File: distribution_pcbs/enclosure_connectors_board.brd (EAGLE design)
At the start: 70 x 40 mm, 15 parts

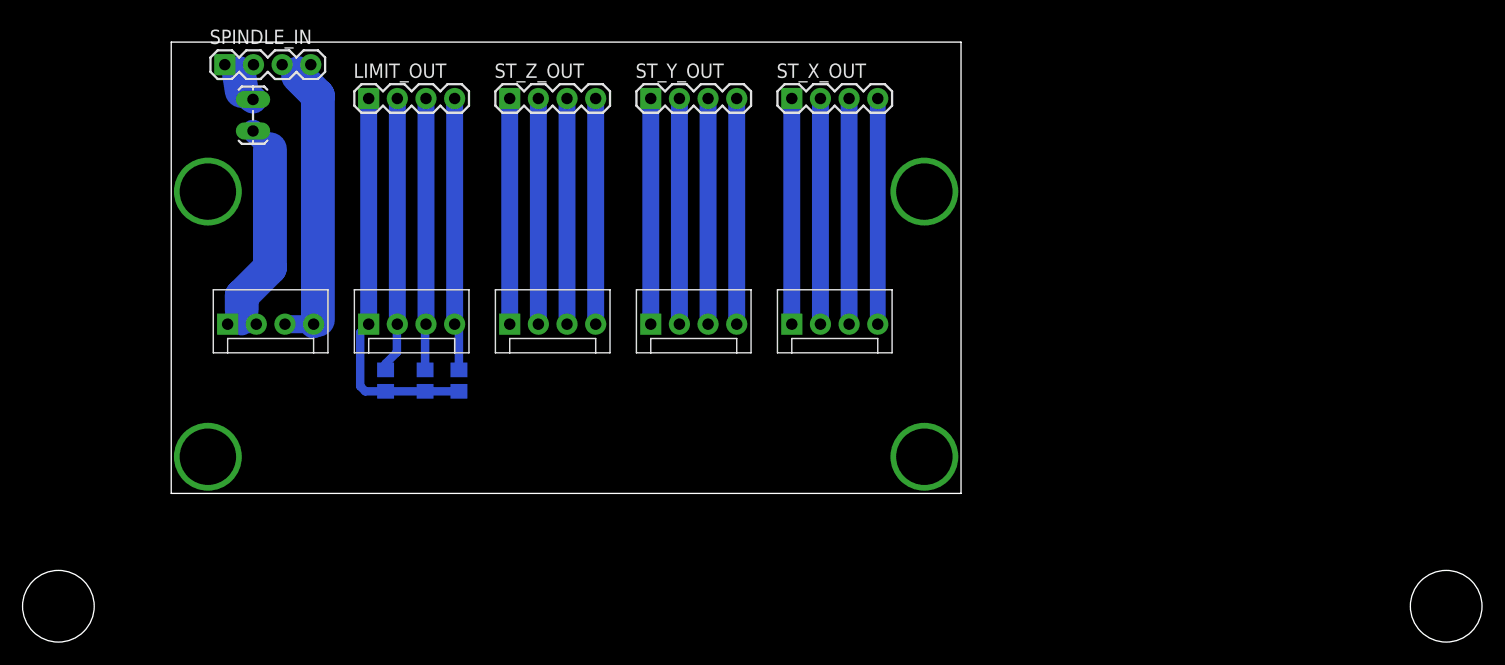
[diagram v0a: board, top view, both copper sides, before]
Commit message: shrink one of the traces to meet clearance requirements
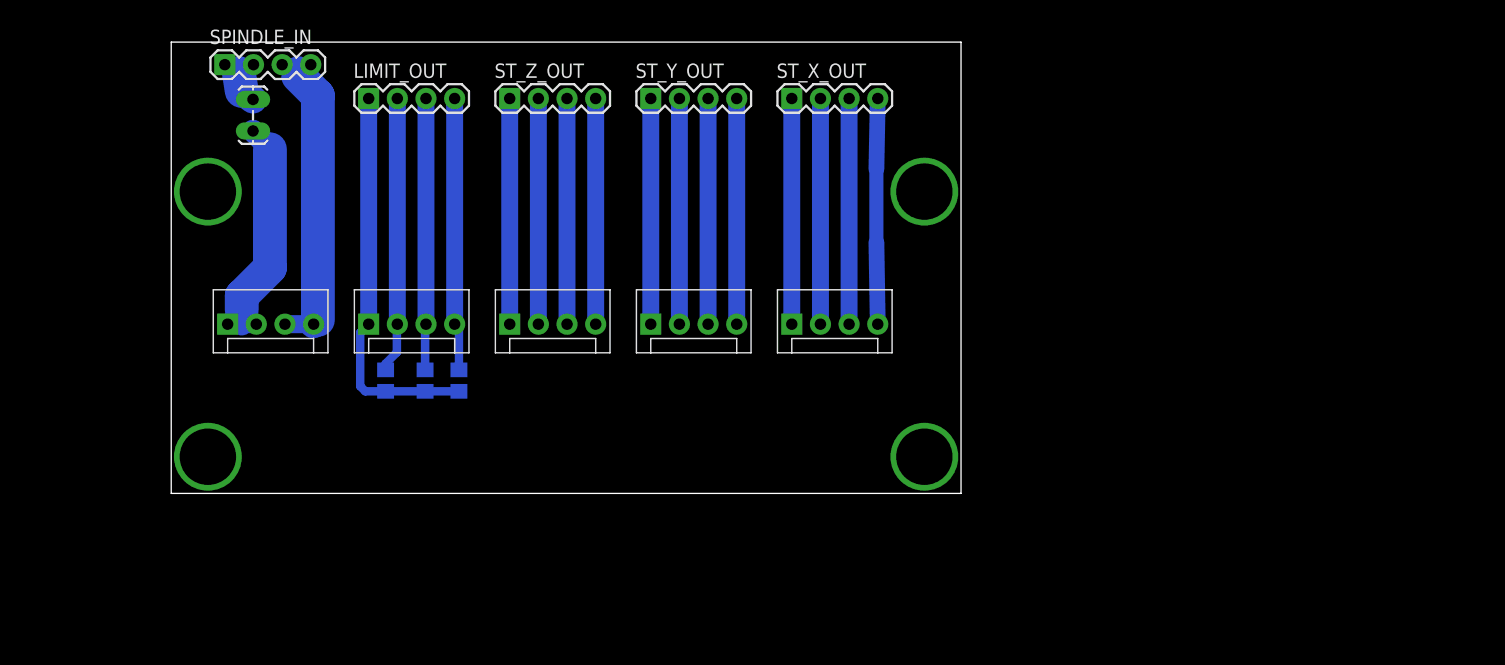
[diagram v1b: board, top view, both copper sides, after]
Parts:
- removed U$1: (no value), helpers:ALIGNMENT_HOLES
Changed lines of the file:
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@@
 <param name="mtCopper" value="0.035mm 0.035mm 0.035mm 0.035mm 0.035mm 0.035mm 0.035mm 0.035mm 0.035mm 0.035mm 0.035mm 0.035mm 0.035mm 0.035mm 0.035mm 0.035mm"/>
 <param name="mtIsolate" value="1.5mm 0.15mm 0.2mm 0.15mm 0.2mm 0.15mm 0.2mm 0.15mm 0.2mm 0.15mm 0.2mm 0.15mm 0.2mm 0.15mm 0.2mm"/>
-<param name="mdWireWire" value="16mil"/>
-<param name="mdWirePad" value="16mil"/>
-<param name="mdWireVia" value="16mil"/>
-<param name="mdPadPad" value="16mil"/>
-<param name="mdPadVia" value="16mil"/>
-<param name="mdViaVia" value="16mil"/>
-<param name="mdSmdPad" value="16mil"/>
-<param name="mdSmdVia" value="16mil"/>
-<param name="mdSmdSmd" value="16mil"/>
+<param name="mdWireWire" value="20mil"/>
+<param name="mdWirePad" value="20mil"/>
+<param name="mdWireVia" value="20mil"/>
+<param name="mdPadPad" value="20mil"/>
+<param name="mdPadVia" value="20mil"/>
+<param name="mdViaVia" value="20mil"/>
+<param name="mdSmdPad" value="20mil"/>
+<param name="mdSmdVia" value="20mil"/>
+<param name="mdSmdSmd" value="20mil"/>
 <param name="mdViaViaSameLayer" value="8mil"/>
 <param name="mnLayersViaInSmd" value="2"/>
@@
 <element name="C3" library="rcl" package="C0805" value="" x="19" y="10" rot="MR270"/>
 <element name="LIMIT_IN" library="SparkFun-Connectors" package="MOLEX-1X4" value="" x="17.5" y="15"/>
-<element name="U$1" library="helpers" package="ALIGNMENT_HOLES" value="" x="0" y="0"/>
 </elements>
 <signals>
@@
 <contactref element="ST_X_IN" pad="4"/>
 <contactref element="ST_X_OUT" pad="4"/>
-<wire x1="62.62" y1="15" x2="62.62" y2="35" width="1.4" layer="16"/>
+<wire x1="62.62" y1="35" x2="62.5" y2="28.75" width="1.4" layer="16"/>
+<wire x1="62.5" y1="28.75" x2="62.5" y2="22.25" width="1.25" layer="16"/>
+<wire x1="62.5" y1="22.25" x2="62.62" y2="15" width="1.4" layer="16"/>
 </signal>
 <signal name="N$2">

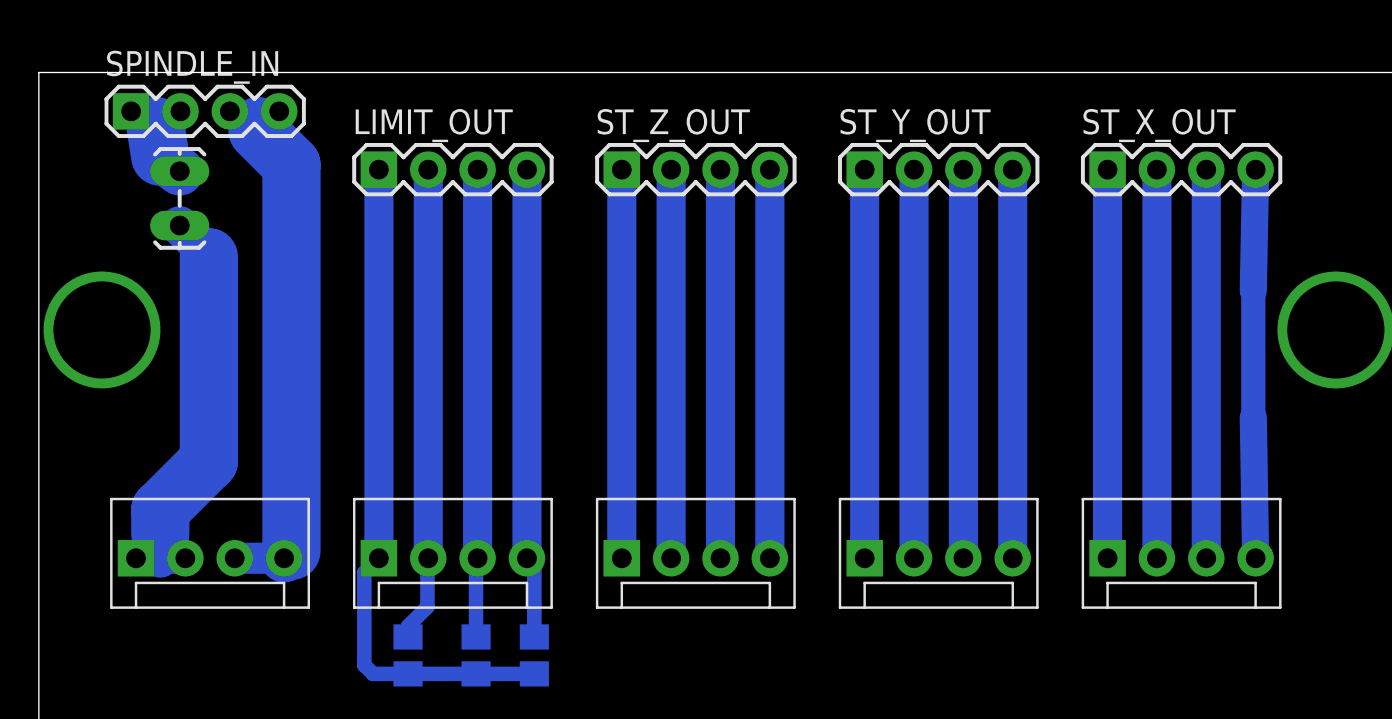
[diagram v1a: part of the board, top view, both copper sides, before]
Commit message: change widths and board dimensions
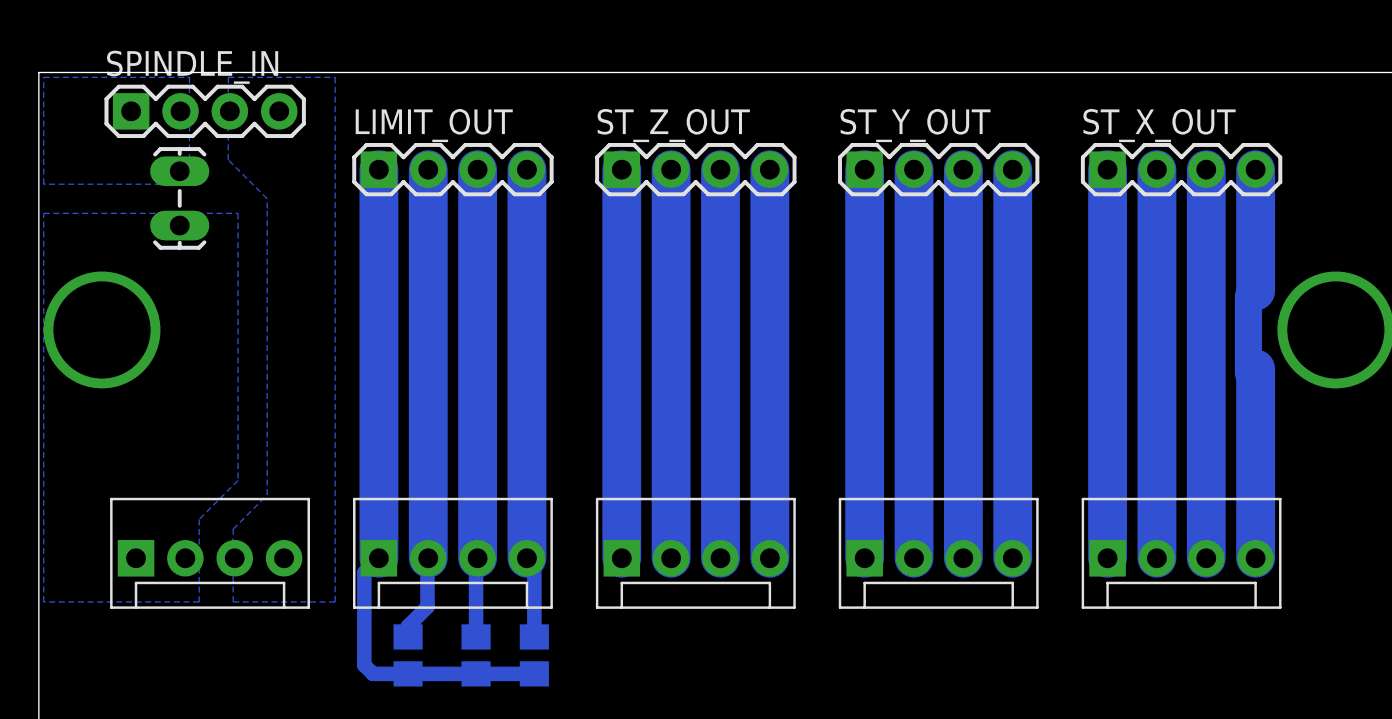
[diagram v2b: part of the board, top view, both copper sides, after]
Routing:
- net SPINDLE_+: track 28.7 -> 0.00 mm
- net SPINDLE_MINUS2: track 21.3 -> 0.00 mm
- net SPINDLE_MINUS: track 5.80 -> 0.00 mm
- net N$1: track 20.0 -> 20.9 mm
- added copper zone on layer 16, net SPINDLE_+
- added copper zone on layer 16, net SPINDLE_MINUS
- added copper zone on layer 16, net SPINDLE_MINUS2
